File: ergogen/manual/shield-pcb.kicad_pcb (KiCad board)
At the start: 2 copper layers, 118.1 x 90.8 mm, 26 parts

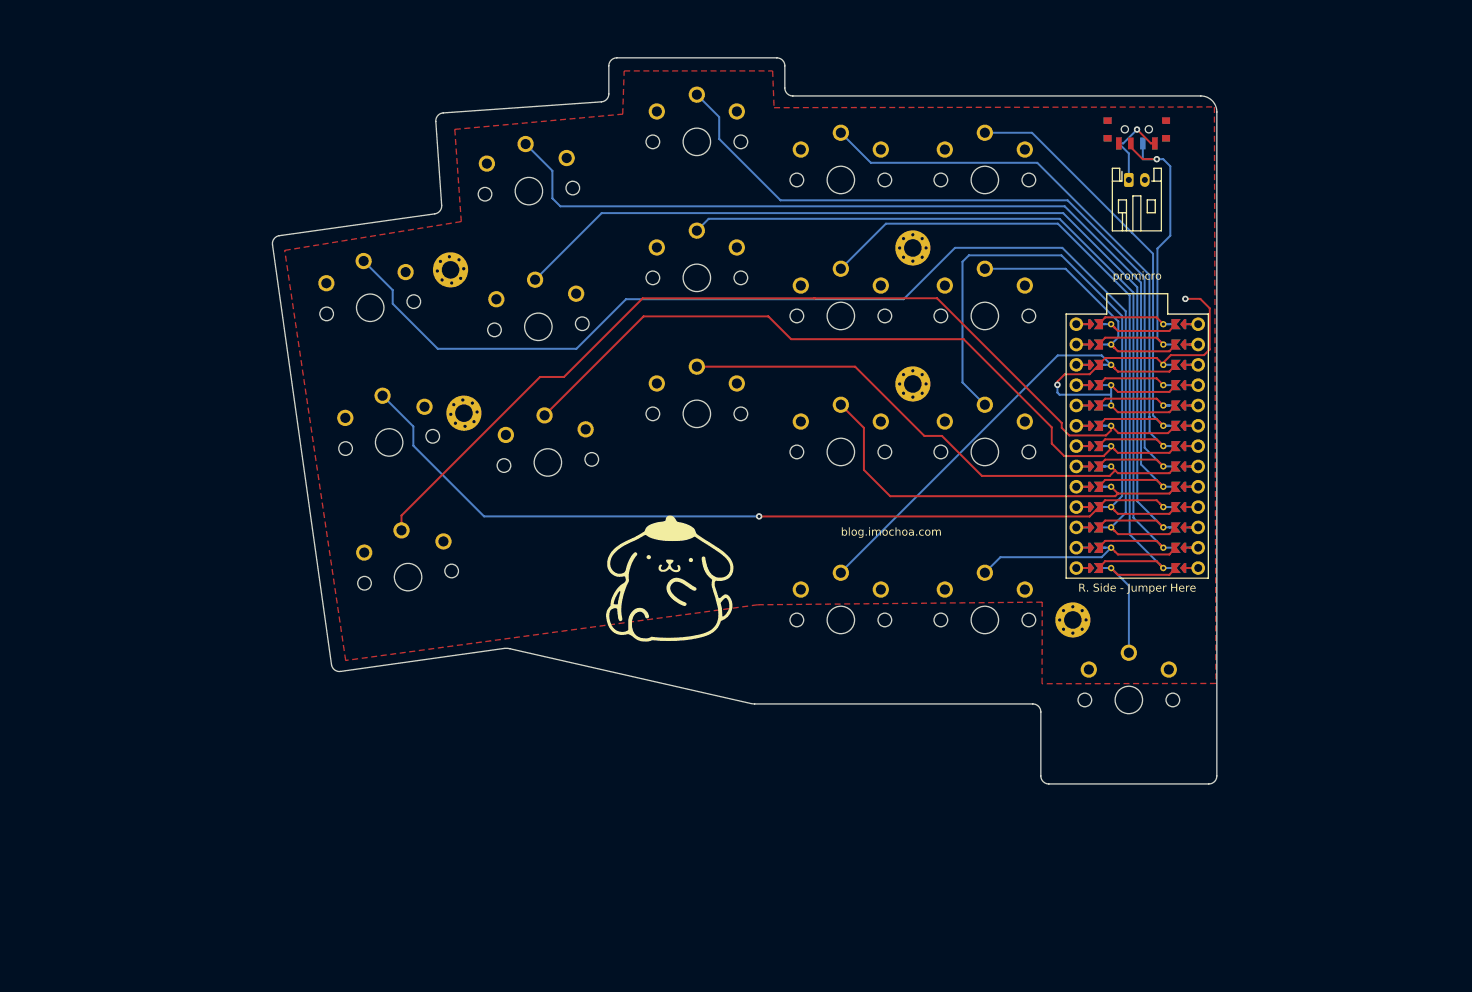
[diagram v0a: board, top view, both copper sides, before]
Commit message: hw: wip ergogen/kicad pcb updates + build scripts
- ergogen config + generated outputs (outlines, cases, pcb) regenerated.
- manual pcb work: shield-pcb routing session, dsn, round-tracks config.
- build.sh / rebuild.sh / bak.script.sh: local build helper scripts.
- ergogen/old-config.yaml: reference from previous iteration.
- pics/: sticker/art assets.
- flake.lock: nix lock bump.
- gitignore freerouting jar, editor .history, gerbers, Untitled artifacts.
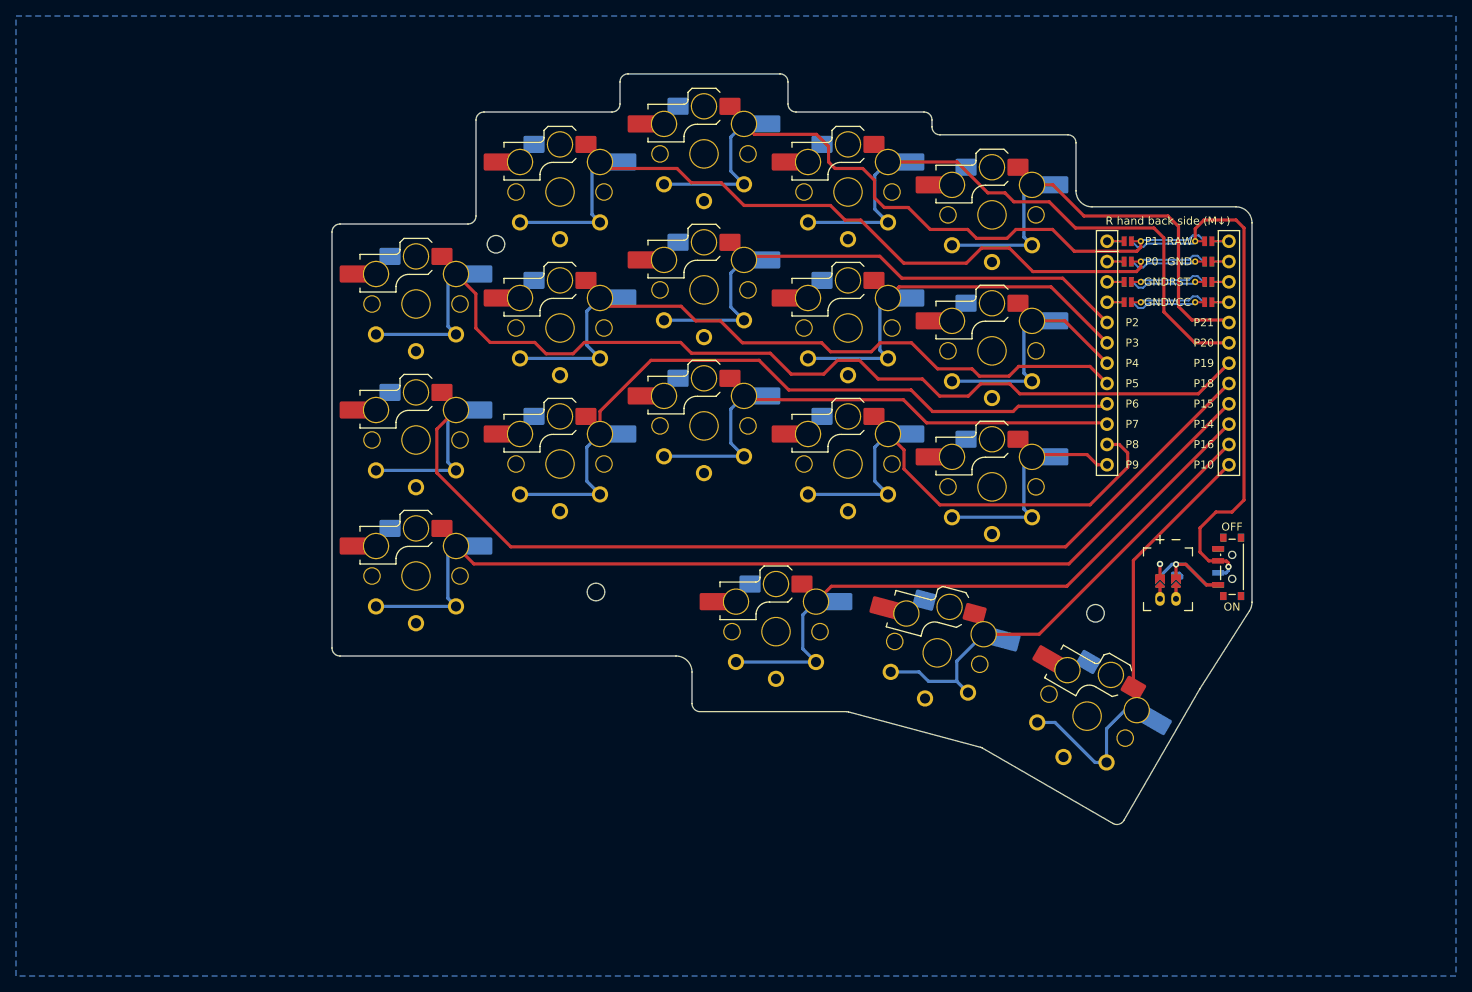
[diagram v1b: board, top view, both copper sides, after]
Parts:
- removed MCU: , ProMicro
- removed T1: , Button_Switch_SMD:SW_SPDT_PCM12
- removed _10, _6, _7, _8, _9: , MountingHole_2.2mm_M2_Pad_Via
- removed _2: , Connector_JST:JST_PH_S2B-PH-K_1x02_P2.00mm_Horizontal
- added JST1: , ceoloide:battery_connector_jst_ph_2, F.Cu at (244.0, 152.9)
- added MCU1: , ceoloide:mcu_supermini_nrf52840, F.Cu at (244.0, 120.9)
- added MH1: , ceoloide:mounting_hole_npth, F.Cu at (160.0, 108.5)
- added MH2: , ceoloide:mounting_hole_npth, F.Cu at (172.5, 152.0)
- added MH3: , ceoloide:mounting_hole_npth, F.Cu at (234.9, 154.7)
- added PWR1: , ceoloide:power_switch_smd_side, F.Cu at (252.0, 148.9)
- S1, S10, S11, S12, S13, S14, S15, S16, S17, S18, S2, S3, S4, S5, S6, S7, S8, S9: footprint PG1350 -> ceoloide:switch_choc_v1_v2; moved to B.Cu
- moved S16 8.24 mm to (195.0, 157.0)
- moved S17 7.23 mm to (215.2, 159.6), turned to -15 degrees
- moved S3 5.74 mm to (150.0, 116.0), turned to 0 degrees
- moved S18 5.60 mm to (233.9, 167.5), turned to -30 degrees
- moved S13 4.45 mm to (222.0, 138.9)
- moved S14 4.45 mm to (222.0, 121.9)
- moved S15 4.45 mm to (222.0, 104.9)
- moved S6 3.89 mm to (168.0, 102.0), turned to 0 degrees
- moved S2 3.37 mm to (150.0, 133.0), turned to 0 degrees
- moved S5 2.71 mm to (168.0, 119.0), turned to 0 degrees
- moved S7 1.75 mm to (186.0, 131.2)
- moved S8 1.75 mm to (186.0, 114.2)
- moved S9 1.75 mm to (186.0, 97.2)
- moved S10 1.75 mm to (204.0, 136.0)
- moved S11 1.75 mm to (204.0, 119.0)
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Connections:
- S1 pad 1: GND -> grid-zn_pinky_bottom
- S10 pad 1: GND -> grid-zn_index_bottom
- S11 pad 1: GND -> grid-zn_index_home
- S12 pad 1: GND -> grid-zn_index_top
- S13 pad 1: GND -> grid-zn_inner_bottom
- S14 pad 1: GND -> grid-zn_inner_home
- S15 pad 1: GND -> grid-zn_inner_top
- S16 pad 1: GND -> thumb-zn_near_thumb
- S17 pad 1: GND -> thumb-zn_home_thumb
- S18 pad 1: GND -> thumb-zn_far_thumb
- S2 pad 1: GND -> grid-zn_pinky_home
- S3 pad 1: GND -> grid-zn_pinky_top
- S4 pad 1: GND -> grid-zn_ring_bottom
- S5 pad 1: GND -> grid-zn_ring_home
- S6 pad 1: GND -> grid-zn_ring_top
- S7 pad 1: GND -> grid-zn_middle_bottom
- S8 pad 1: GND -> grid-zn_middle_home
- S9 pad 1: GND -> grid-zn_middle_top
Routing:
- net grid-zn_inner_bottom: track 78.6 -> 31.4 mm
- net grid-zn_index_home: track 88.9 -> 49.2 mm
- net grid-zn_ring_home: track 126.2 -> 88.7 mm
- net grid-zn_middle_home: track 103.3 -> 67.9 mm
- net GND: track 64.9 -> 32.5 mm, vias 2 -> 1
- net thumb-zn_home_thumb: track 28.1 -> 58.5 mm
- net grid-zn_pinky_home: track 109.8 -> 139.8 mm, vias 1 -> 0
- net thumb-zn_far_thumb: track 23.5 -> 52.5 mm
- net RAW: track 43.7 -> 68.2 mm
- net thumb-zn_near_thumb: track 57.6 -> 79.7 mm
- net grid-zn_ring_top: track 123.7 -> 103.8 mm
- net grid-zn_pinky_top: track 148.6 -> 129.2 mm
- net BAT_P: track 0.00 -> 17.1 mm, vias 0 -> 1
- net grid-zn_middle_top: track 103.5 -> 88.9 mm
- net B-: track 11.6 -> 0.00 mm
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- added copper zone on B.Cu, net GND
- removed copper zone on F.Cu, net GND
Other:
- board size 118.1 x 90.8 mm -> 115 x 93.8 mm
- board text removed: "blog.imochoa.com"
